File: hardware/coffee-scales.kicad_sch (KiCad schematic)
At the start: 5 parts, among them J1 Conn_01x04, SW1 SW_Push, U1 Adafruit_Feather_328P, U3 4DIGIT_7SEG, U4 4DIGIT_7SEG

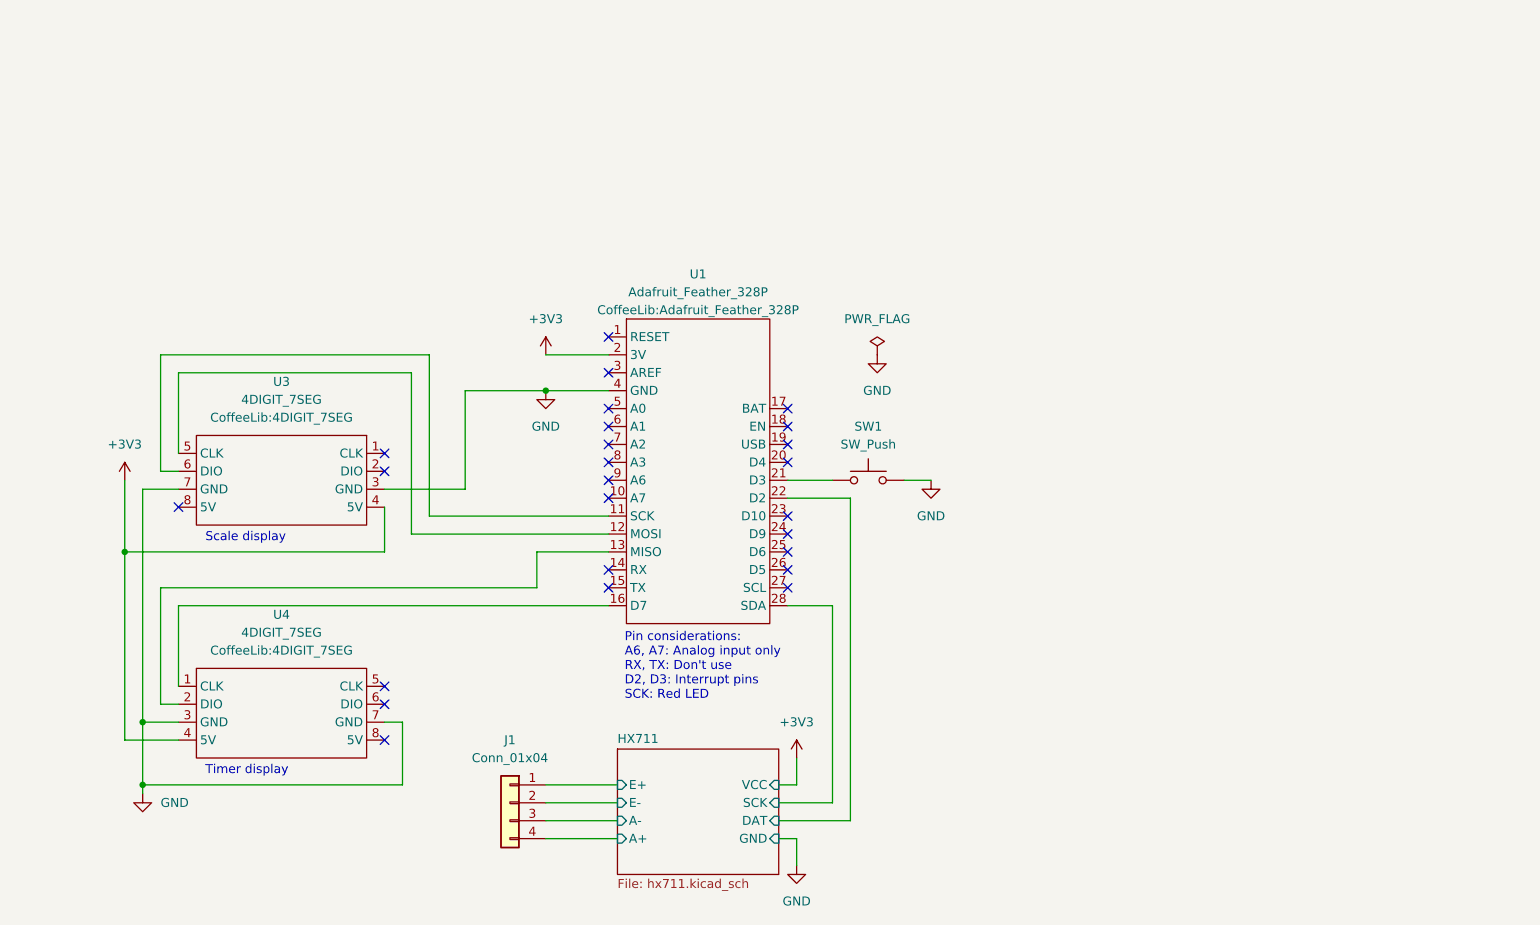
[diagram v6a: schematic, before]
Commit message: Route most of the 328 stuff
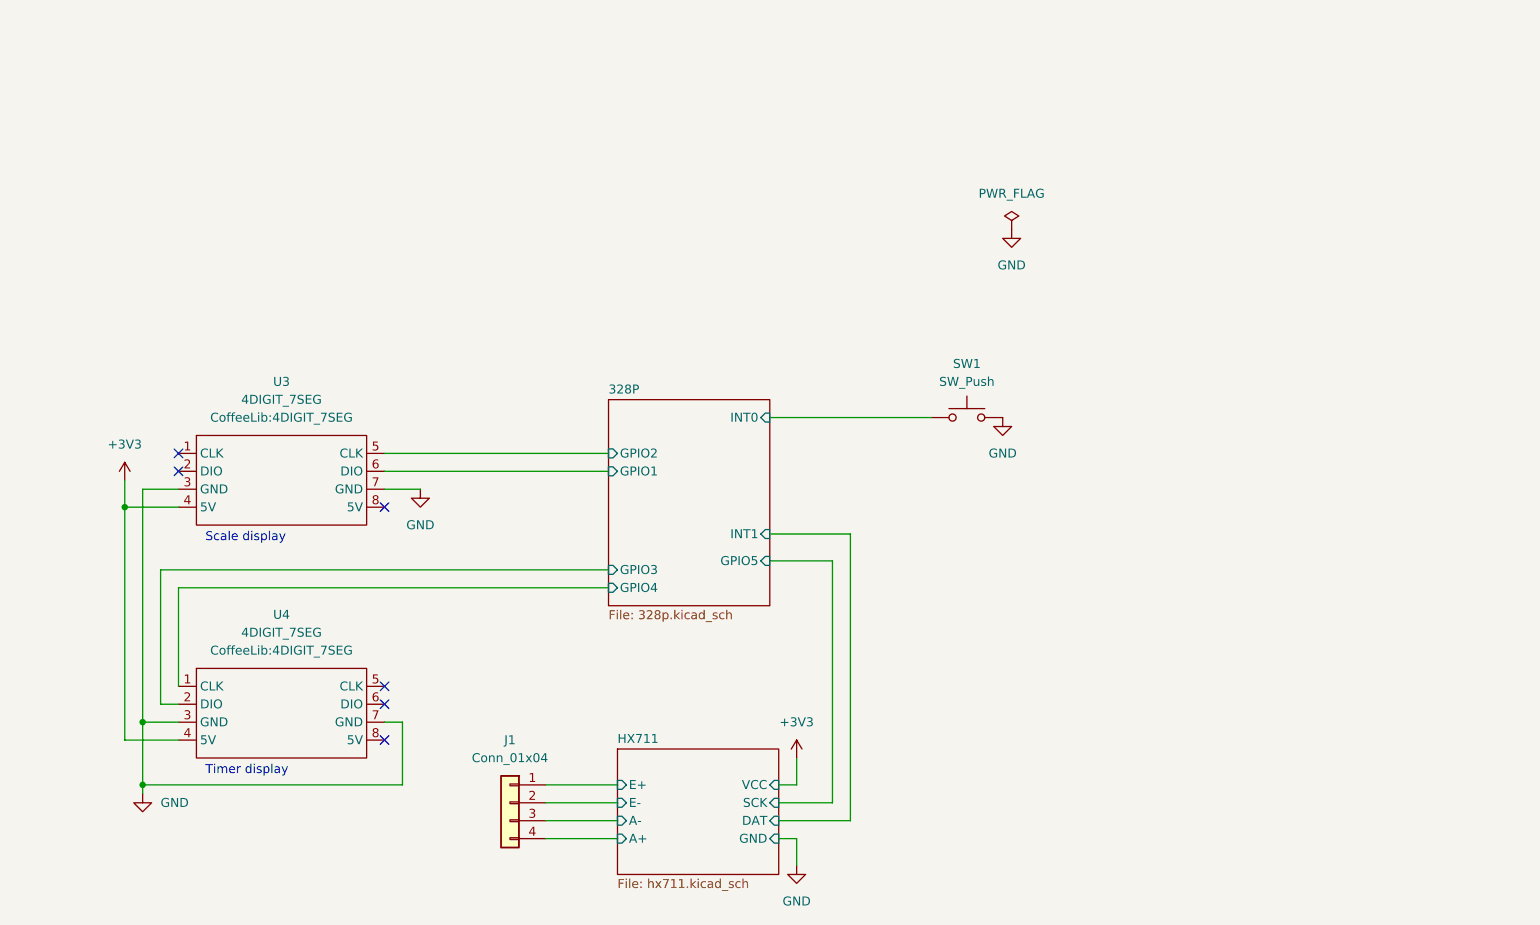
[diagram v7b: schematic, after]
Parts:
- removed U1: Adafruit_Feather_328P, CoffeeLib:Adafruit_Feather_328P, symbol CoffeeLib:Adafruit_Feather_328P
- J1: footprint Connector_PinHeader_2.54mm:PinHeader_1x04_P2.54mm_Vertical -> Connector_PinSocket_2.54mm:PinSocket_1x04_P2.54mm_Horizontal
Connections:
- net 328P/INT0: now reaches SW1.1
- net 328P/GPIO1: now reaches U3.6 (DIO)
- net 328P/GPIO2: now reaches U3.5 (CLK)
- net 328P/GPIO3: now reaches U4.2 (DIO)
- net 328P/GPIO4: now reaches U4.1 (CLK)
- no-connect marks 25 -> 6
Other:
- added sheet 328P (328p.kicad_sch)
- note removed: "Pin considerations: A6, A7: Analog input only RX, TX: Don't use D2, D3: Interrupt pins SCK: Red LED"
- moved on the sheet: SW1

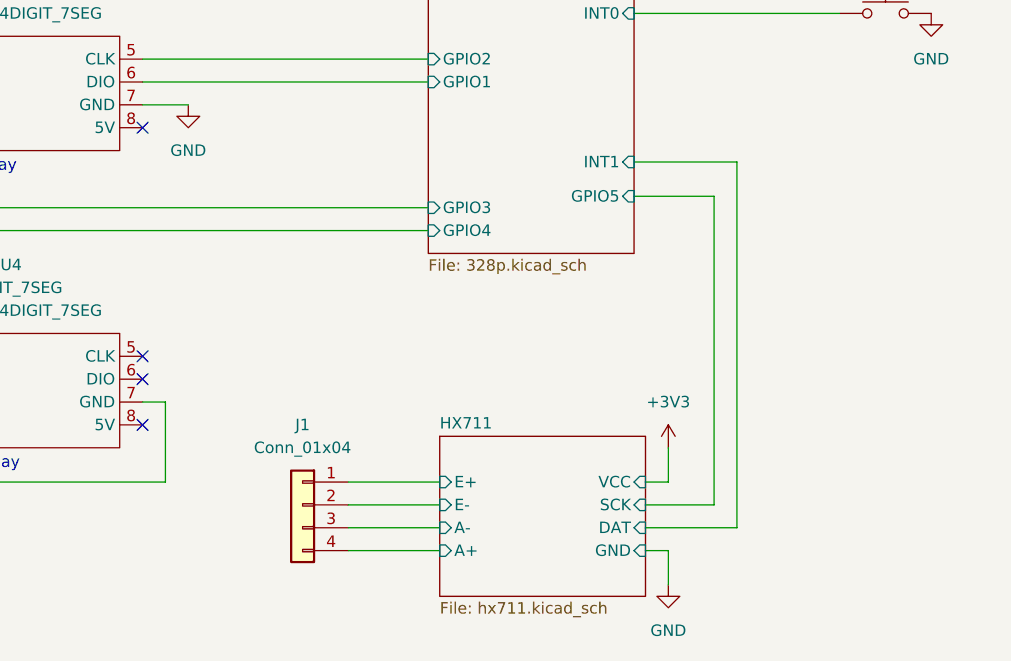
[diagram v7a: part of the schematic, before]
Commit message: Create analog ground plane for HX711
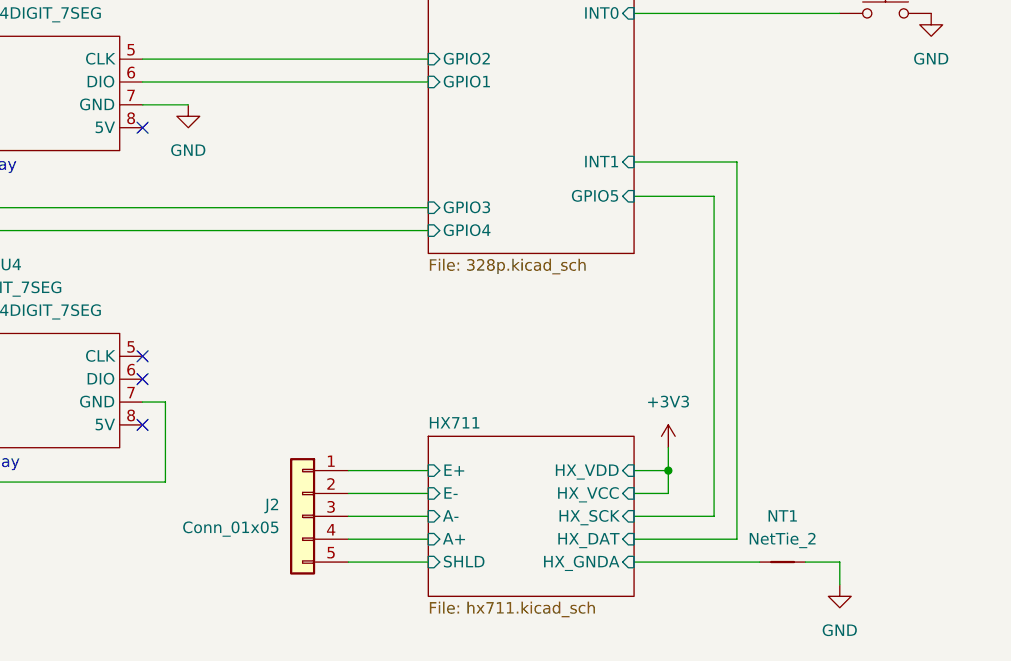
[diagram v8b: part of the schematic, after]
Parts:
- removed J1: Conn_01x04, Connector_PinSocket_2.54mm:PinSocket_1x04_P2.54mm_Horizontal, symbol Connector_Generic:Conn_01x04
- added J2: Conn_01x05, Connector_PinSocket_2.54mm:PinSocket_1x05_P2.54mm_Horizontal, symbol Connector_Generic:Conn_01x05
- added NT1: NetTie_2, NetTie:NetTie-2_SMD_Pad0.5mm, symbol Device:NetTie_2
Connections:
- net GND: now also NT1.2
- net HX711/A+: now also J2.4 (Pin_4)
- net HX711/A-: now also J2.3 (Pin_3)
- net HX711/E+: now also J2.1 (Pin_1)
- net HX711/E-: now also J2.2 (Pin_2)
- new net HX711/HX_GNDA: NT1.1
- new net HX711/SHLD: J2.5 (Pin_5)
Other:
- sheet HX711 ports: added HX_DAT, HX_GNDA, HX_SCK, HX_VCC, HX_VDD, SHLD; removed DAT, GND, SCK, VCC
